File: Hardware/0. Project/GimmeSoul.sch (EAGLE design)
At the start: 15 parts, among them U2 ATMEGA328P-AU

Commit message: Schematic minor improvements
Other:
- note removed: "POWER SUPPLY & BATTERY STATUS MONITOR"
- moved on the sheet: ANALOG, C3, C4, DIGITAL1, DIGITAL2, POWER, R26, U2, ZX1

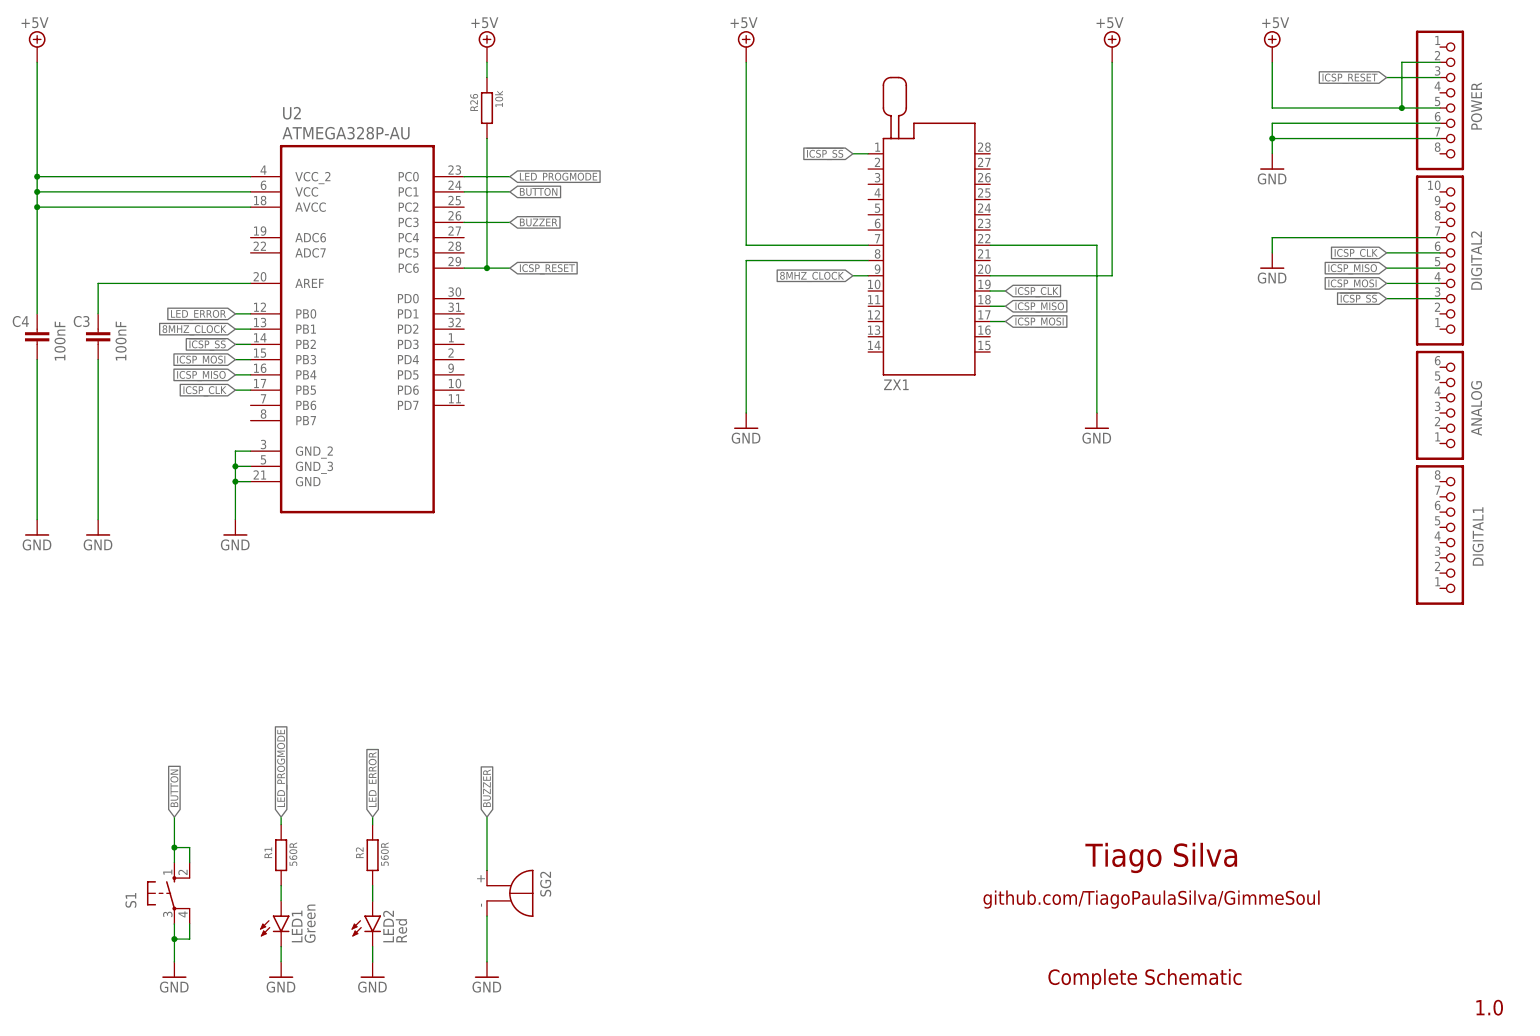
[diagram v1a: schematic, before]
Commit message: Programing Status Effects Updated
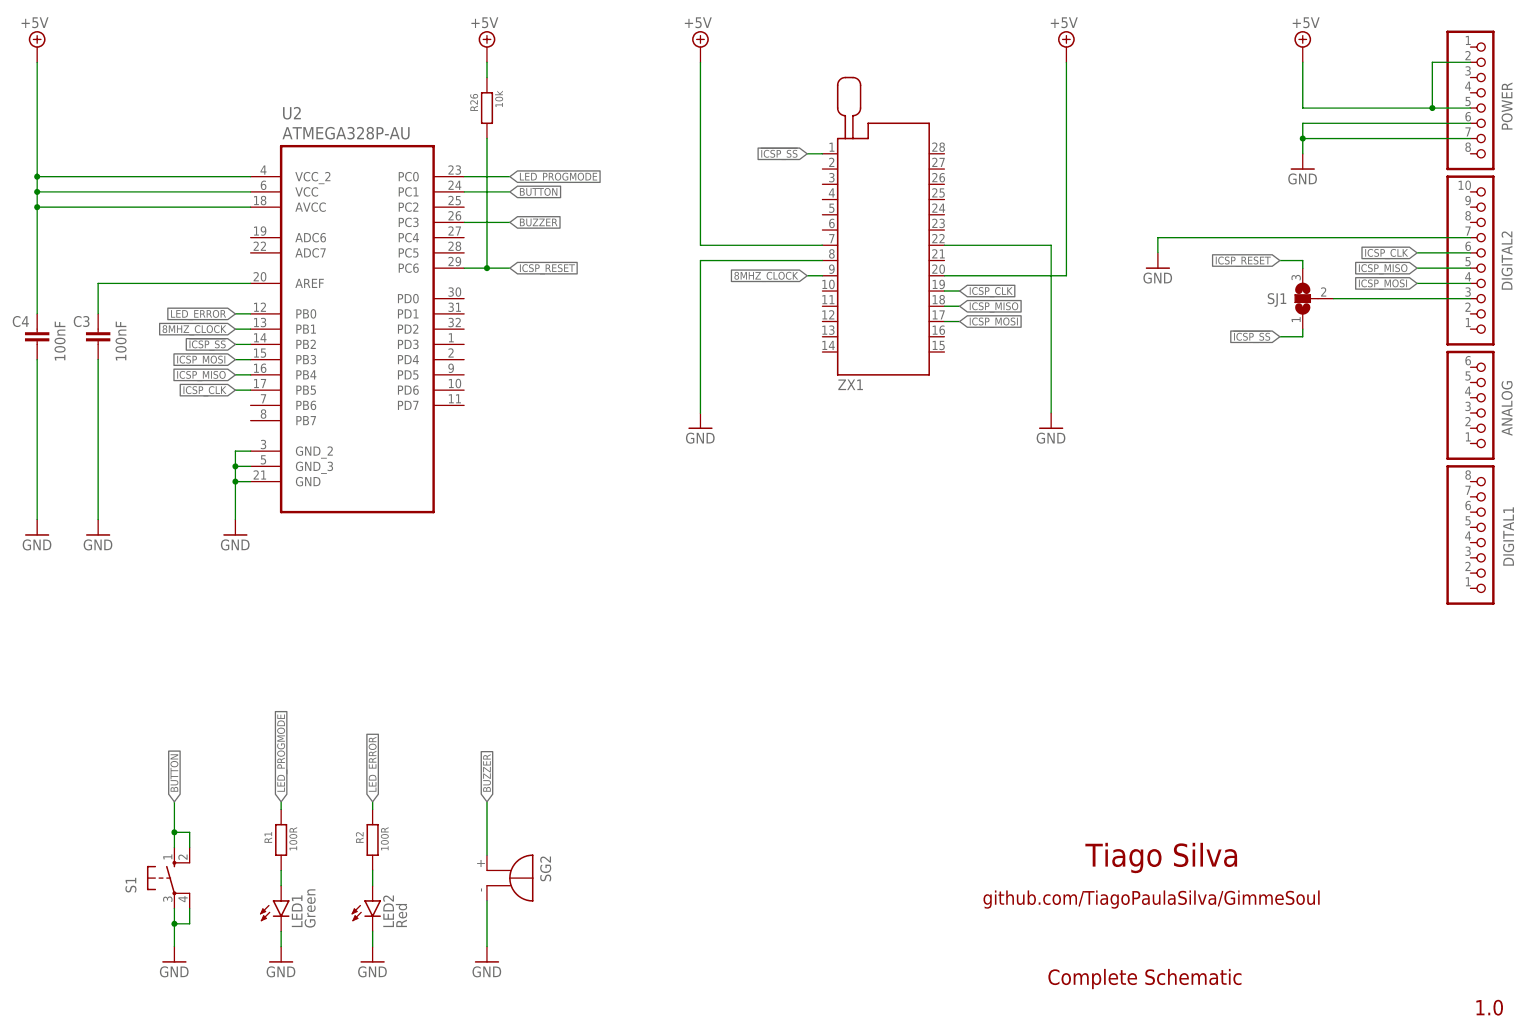
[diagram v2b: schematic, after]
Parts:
- added SJ1: (no value), jumper:SJ2W
- R1, R2: value 560R -> 100R
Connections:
- net !ICSP_SS: now also SJ1.1; no longer DIGITAL2.3
- net ICSP_RESET: now also DIGITAL2.3, SJ1.2, SJ1.3; no longer POWER.3
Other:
- moved on the sheet: ANALOG, DIGITAL1, DIGITAL2, LED1, LED2, POWER, R1, R2, S1, SG2, ZX1

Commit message: Jumper SJ1 and Button Reset S1 added
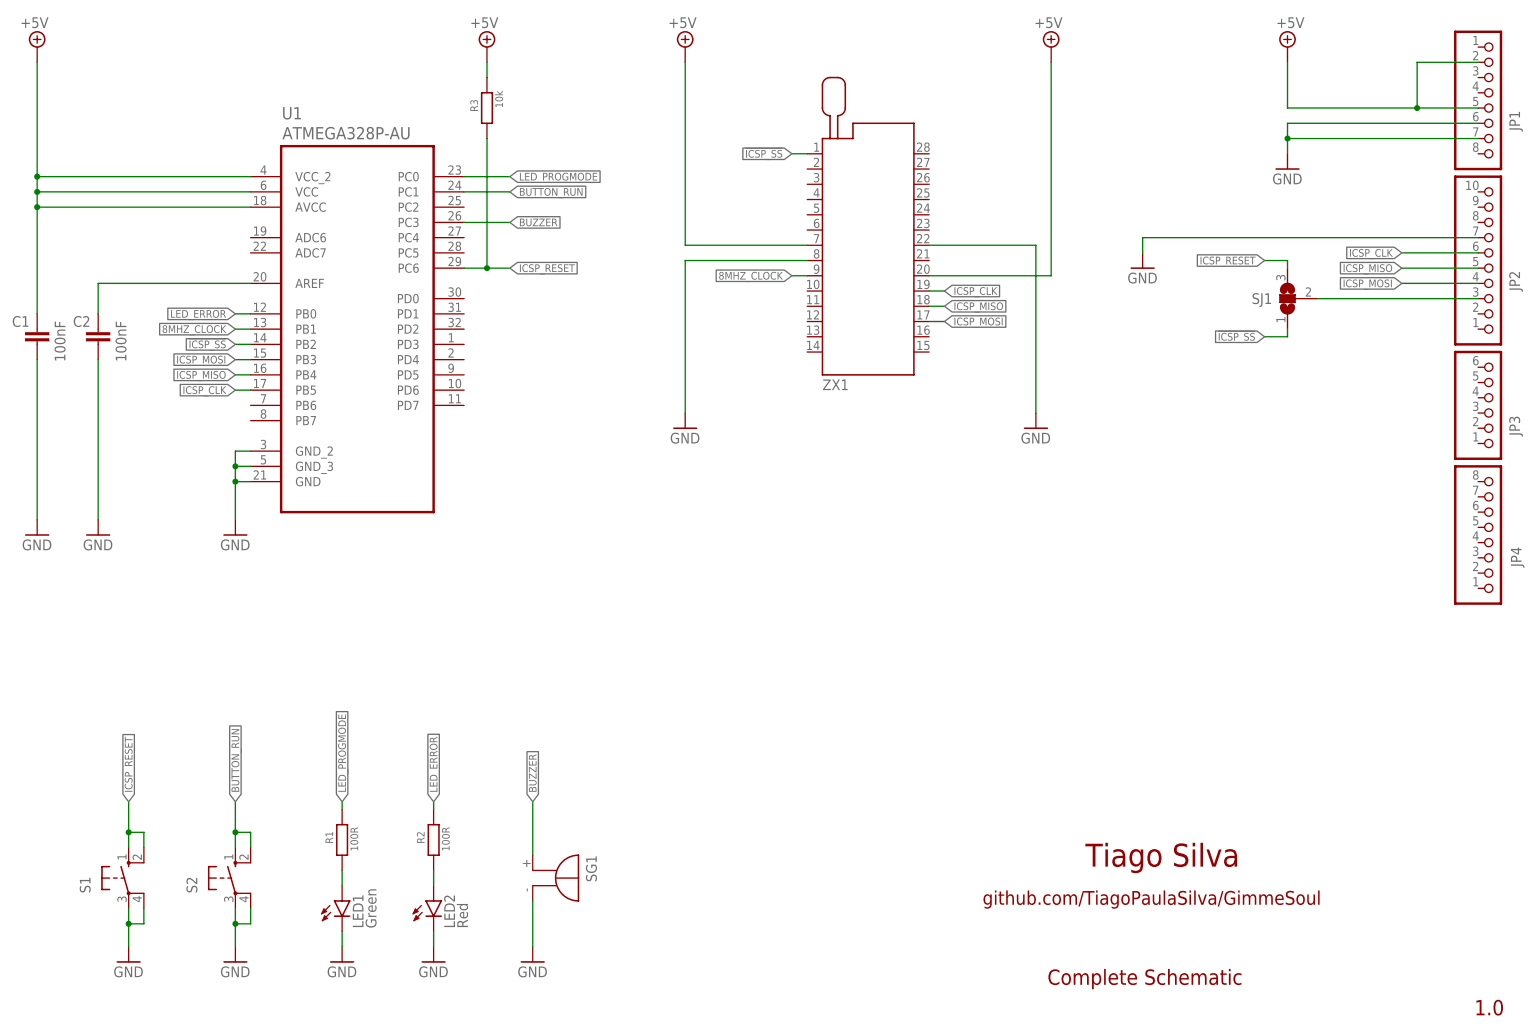
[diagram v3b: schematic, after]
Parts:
- removed ANALOG: (no value), SmartPrj:PINHD-1X6
- removed DIGITAL1, POWER: (no value), SmartPrj:PINHD-1X8
- removed DIGITAL2: (no value), SmartPrj:PINHD-1X10_ARD
- removed SG2: EB2505, buzzer:EB2505
- added JP1, JP4: (no value), SmartPrj:PINHD-1X8
- added JP2: (no value), SmartPrj:PINHD-1X10_ARD
- added JP3: (no value), SmartPrj:PINHD-1X6
- added S2: (no value), switch-omron:10-XX
- added SG1: EB2505, buzzer:EB2505
- renumbered C3 to C2, C4 to C1, R26 to R3, U2 to U1
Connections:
- removed net BUTTON: S1.S, S1.S1, U1.PC1
- new net BUTTON_RUN: S2.S, S2.S1, U1.PC1
- net +5V: now also JP1.2, JP1.5; no longer POWER.2, POWER.5
- net BUZZER: now also SG1.+; no longer SG2.+
- net GND: now also JP1.6, JP1.7, JP2.7, S2.P, S2.P1, SG1.-; no longer DIGITAL2.7, POWER.6, POWER.7, SG2.-
- net ICSP_CLK: now also JP2.6; no longer DIGITAL2.6
- net ICSP_MISO: now also JP2.5; no longer DIGITAL2.5
- net ICSP_MOSI: now also JP2.4; no longer DIGITAL2.4
- net ICSP_RESET: now also JP2.3, S1.S, S1.S1; no longer DIGITAL2.3
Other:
- note added: "*"
- note added: "SJ1 - Position 2-1: Position for conventional use of GimmeSoul. This position allows you to standalone programming the bootloader of other ATmega."
- note added: "SJ1 - Position 2-3: On the first use of the GimmeSoul, this position allows you to programming the U1 bootloader using an Arduino UNO."
- moved on the sheet: LED1, LED2, R1, R2, S1, SJ1, ZX1

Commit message: External power supply support added
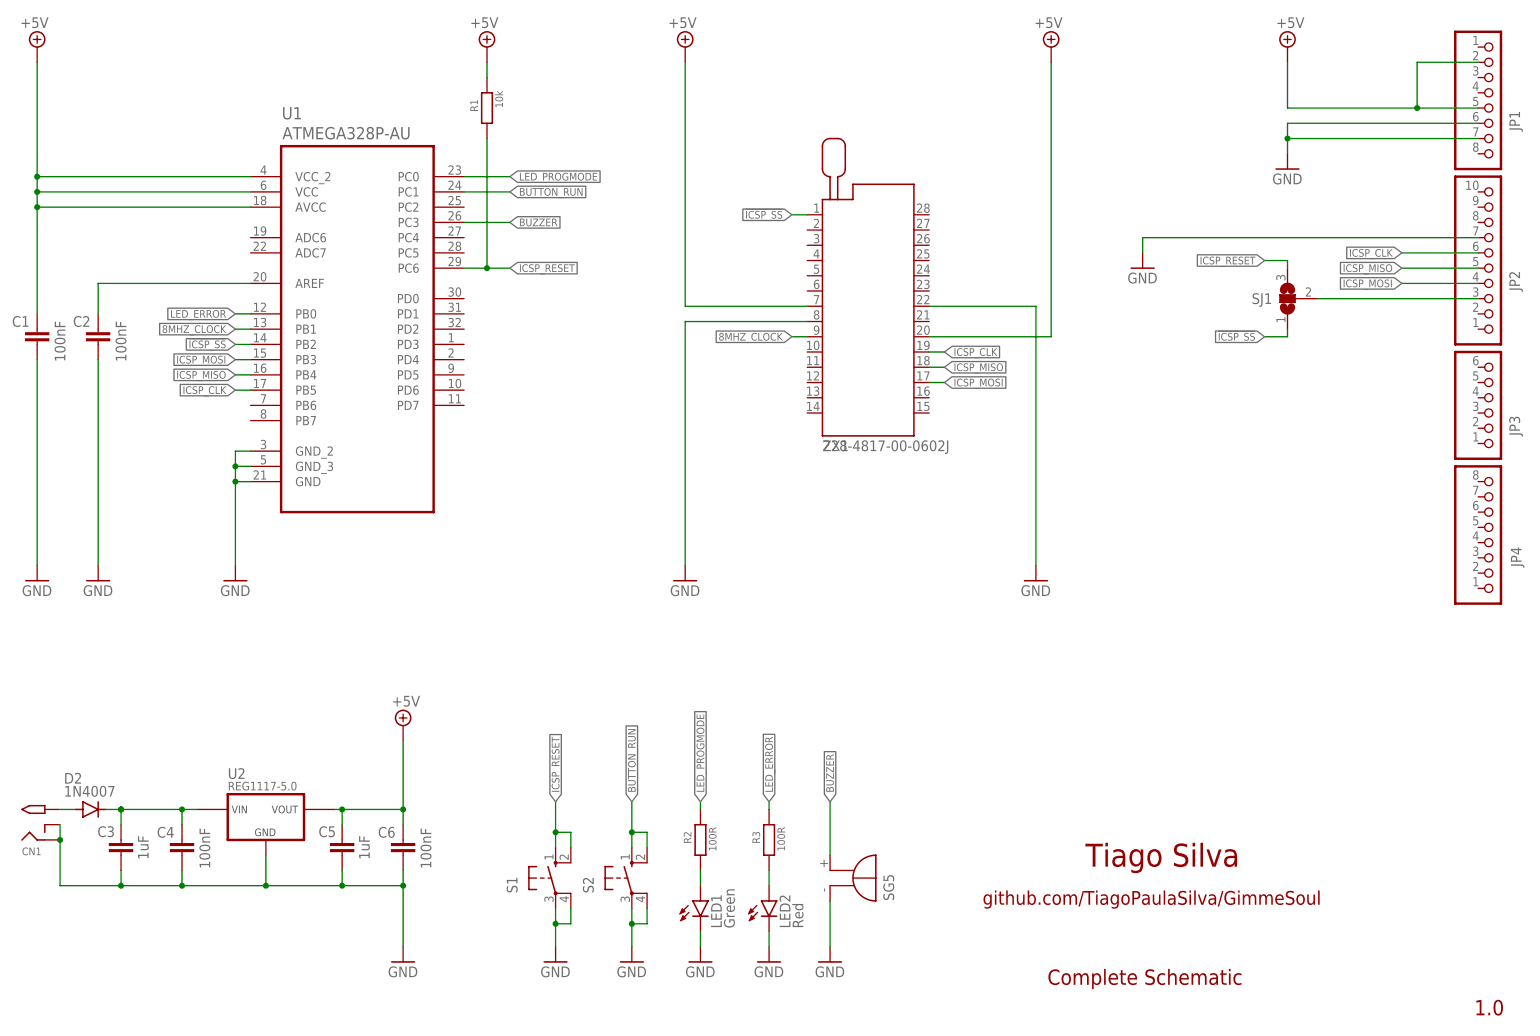
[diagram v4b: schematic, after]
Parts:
- removed SG1: EB2505, buzzer:EB2505
- added C3, C5: 1uF, rcl:C-EUC0805
- added C4, C6: 100nF, rcl:C-EUC0805
- added CN1: 2.1MMJACKTHM, adafruit:2.1MMJACKTHM
- added D2: 1N4007, diode:DIODE-SOD123
- added SG5: 5V PASSIVE, buzzer:F/QMBIII
- added U2: REG1117-5.0, REG1117:REG1117
- R1: value 100R -> 10k
- R3: value 10k -> 100R
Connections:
- new net N$2: CN1.TIP, D2.A
- new net N$4: C3.1, C4.1, D2.C, U2.VIN
- new net N$5: JP2.3, SJ1.2
- net +5V: now also C5.1, C6.1, R1.1, U2.VOUT; no longer R3.1
- net BUZZER: now also SG5.-; no longer SG1.+
- net GND: now also C3.2, C4.2, C5.2, C6.2, CN1.RING, CN1.RING_SW, SG5.+, U2.GND; no longer SG1.-
- net ICSP_RESET: now also R1.2; no longer JP2.3, R3.2, SJ1.2
- net LED_ERROR: now also R3.1; no longer R2.1
- net LED_PROGMODE: now also R2.1; no longer R1.1
- net N$1: now also R2.2; no longer R1.2
- net N$3: now also R3.2; no longer R2.2
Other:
- note added: "EXTERNAL POWER SUPPLY"
- moved on the sheet: LED1, LED2, R1, R2, R3, S1, S2, ZX1
